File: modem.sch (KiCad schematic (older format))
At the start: 26 parts

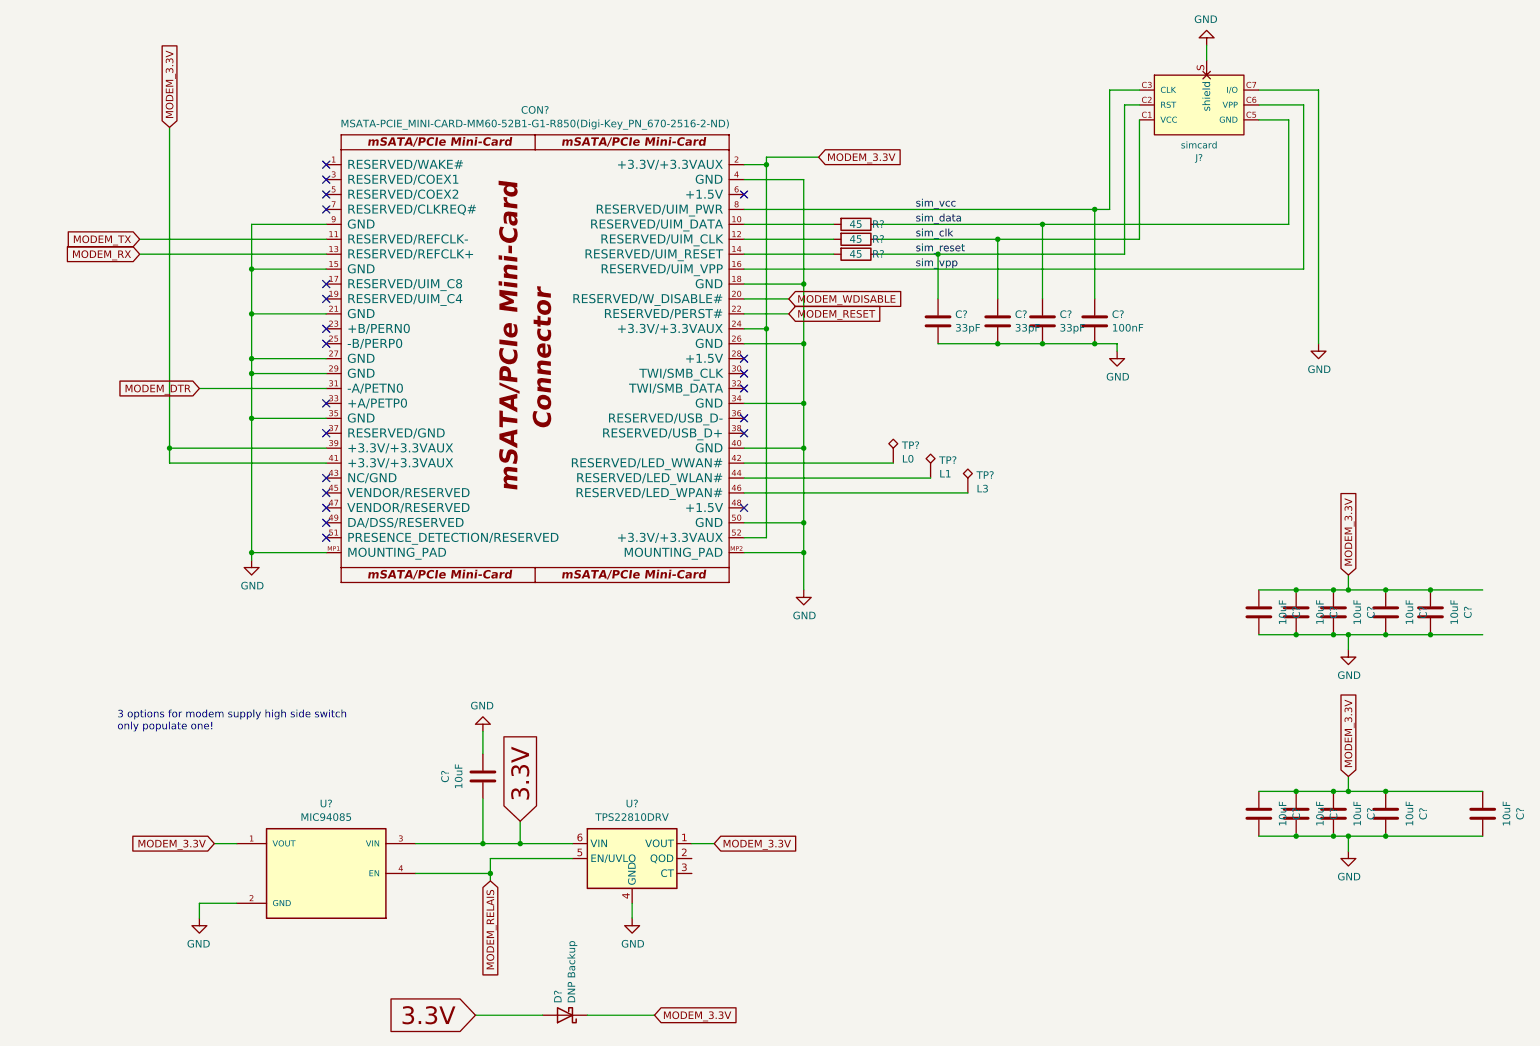
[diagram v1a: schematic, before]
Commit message: Esp32 & Canbus Sch. edited.
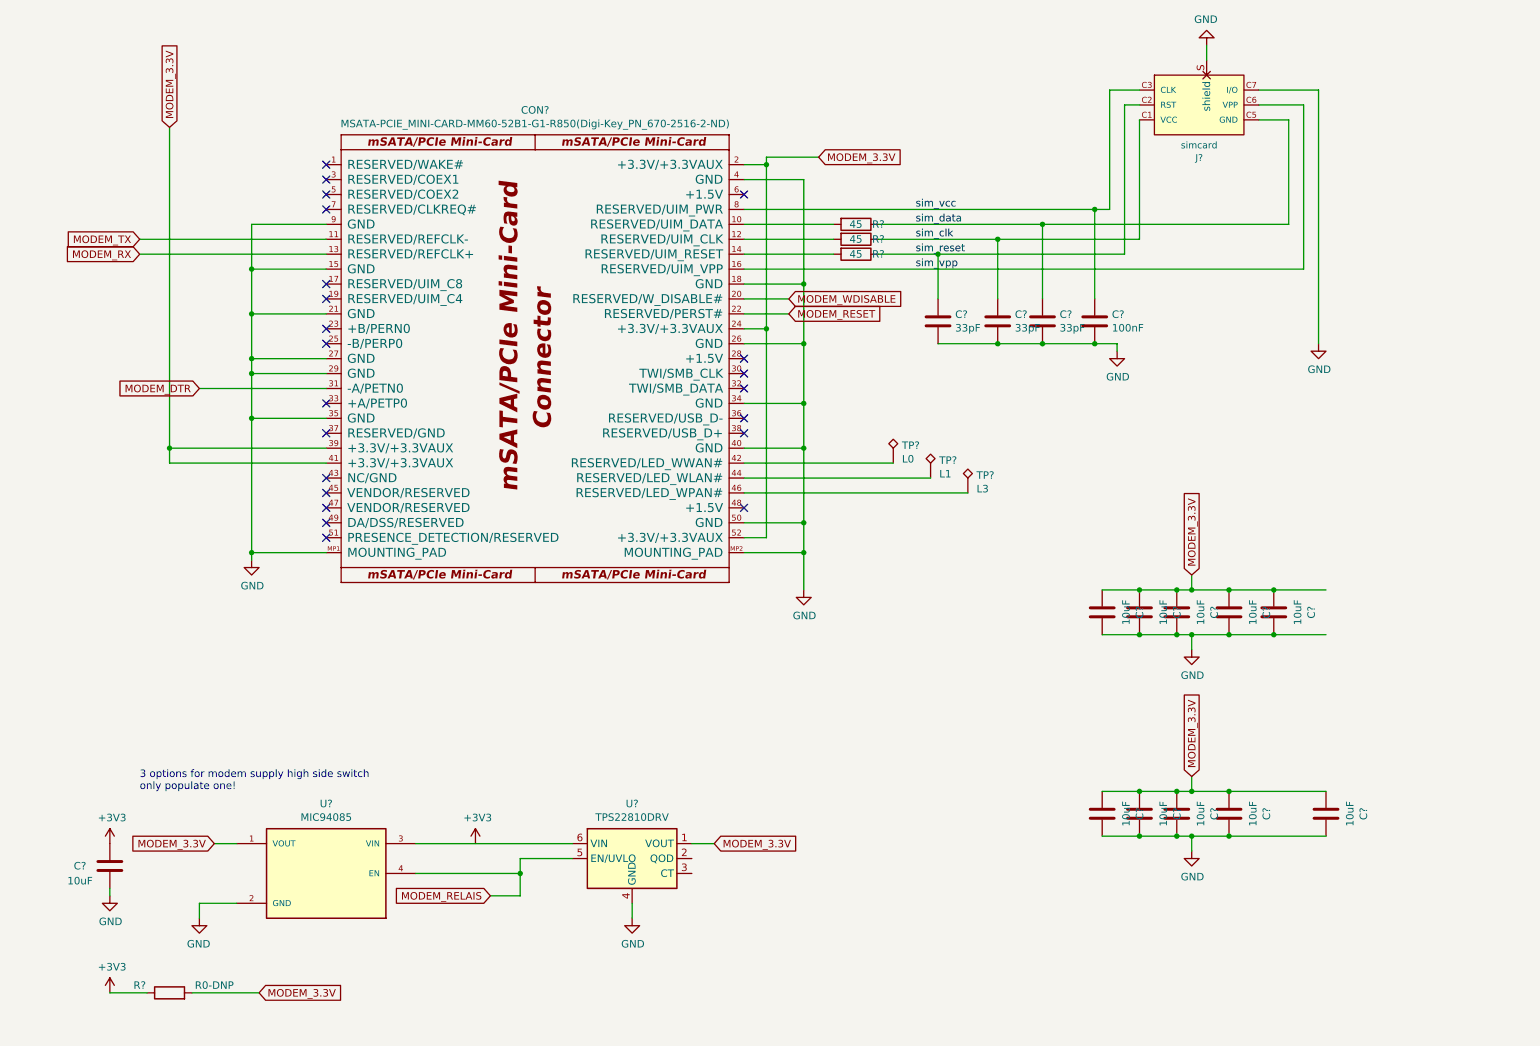
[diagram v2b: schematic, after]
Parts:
- removed C?: 10uF, Capacitor_SMD:C_1206_3216Metric, symbol Device:C
- removed D?: DNP Backup, Diode_SMD:D_SOD-123, symbol Device:D_Schottky
- added C?: 10uF, Capacitor_SMD:C_0603_1608Metric, symbol Device:C
- added R?: R0-DNP, Resistors:0603, symbol Device:R
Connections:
- net GND: now also C?.2
- net MODEM_3.3V: now also R?.2
- net 3.3V: no longer names the net of U?.3 (VIN), U?.6 (VIN)
- new net +3V3: C?.1, R?.1
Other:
- moved on the sheet: C?

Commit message: Modem schematic updated.
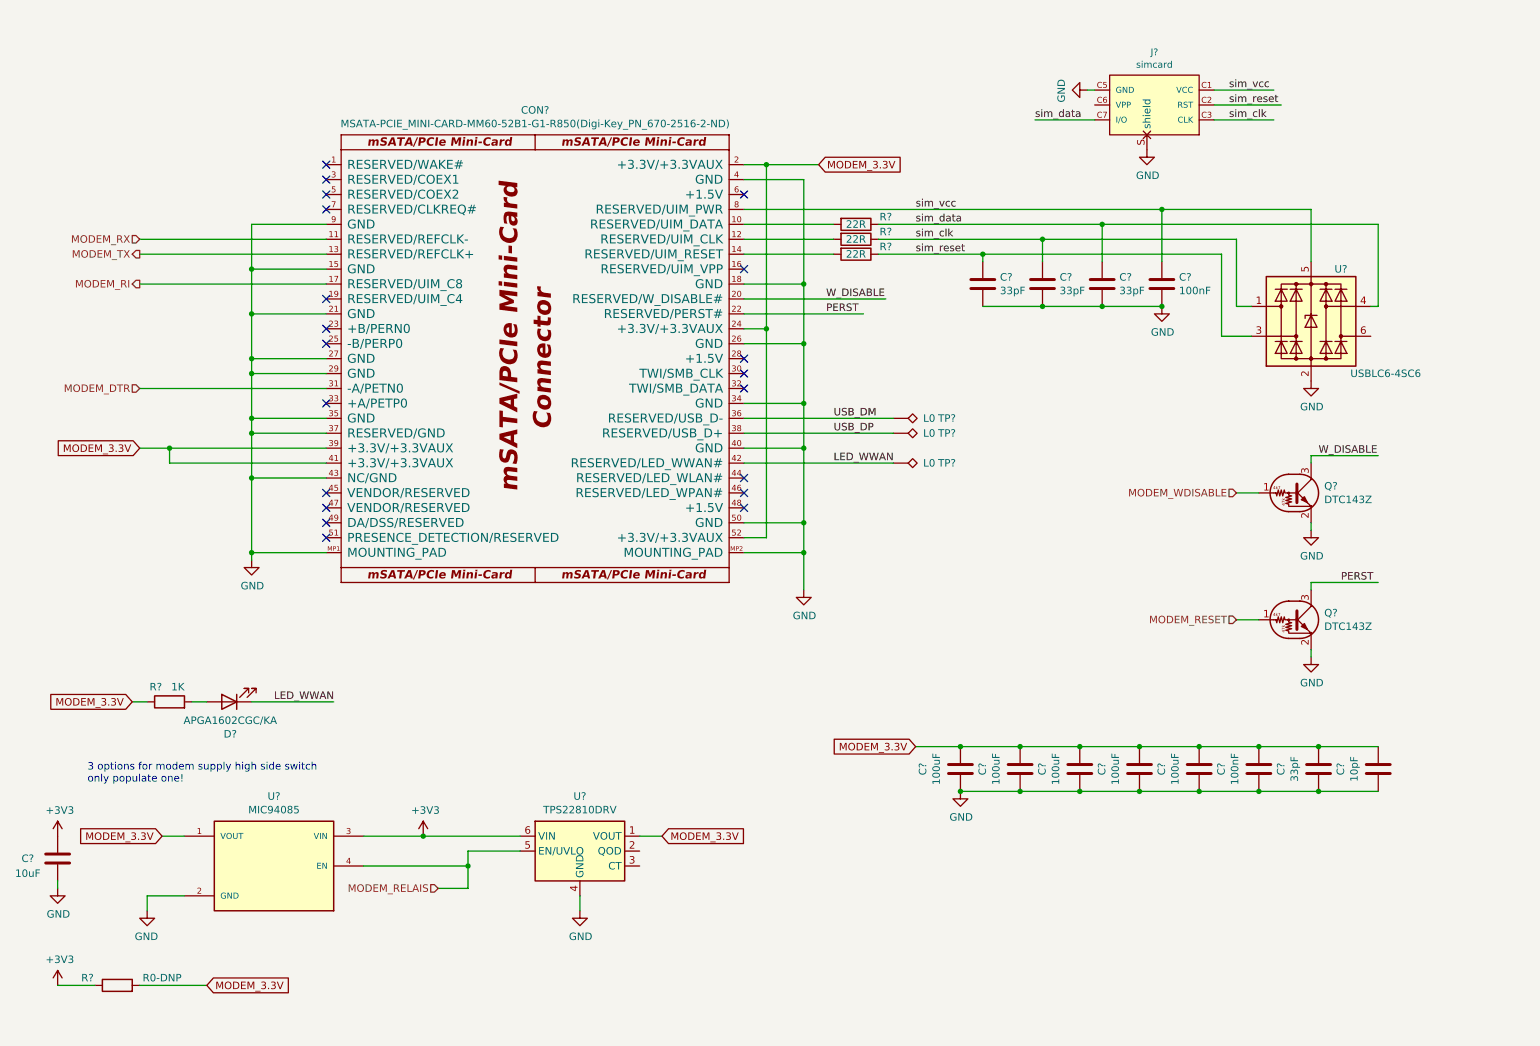
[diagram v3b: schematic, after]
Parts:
- removed C? (x10): 10uF, Capacitor_SMD:C_1206_3216Metric, symbol Device:C
- removed TP?: L0, OLIMEX_TestPoints-FP:TP_SMD, symbol Connector:TestPoint_Alt
- removed TP?: L1, OLIMEX_TestPoints-FP:TP_SMD, symbol Connector:TestPoint_Alt
- removed TP?: L3, OLIMEX_TestPoints-FP:TP_SMD, symbol Connector:TestPoint_Alt
- added C?: 10pF, Capacitor_SMD:C_0603_1608Metric, symbol Device:C
- added C?: 100nF, Capacitor_SMD:C_0603_1608Metric, symbol Device:C
- added C? (x5): 100uF, Capacitor_SMD:C_1206_3216Metric, symbol Device:C
- added C?: 33pF, Capacitor_SMD:C_0603_1608Metric, symbol Device:C
- added D?: APGA1602CGC/KA, LED_SMD:LED_0603_1608Metric, symbol Device:LED
- added Q? (x2): DTC143Z, symbol Transistor_BJT:DTC143Z
- added R?: 1K, Resistor_SMD:R_0603_1608Metric, symbol Device:R
- added TP? (x3): L0, OLIMEX_TestPoints-FP:TP_SMD, symbol Connector:TestPoint_Alt
- added U?: USBLC6-4SC6, Package_TO_SOT_SMD:SOT-23-6, symbol Power_Protection:USBLC6-4SC6
- R? (x3): value 45 -> 22R
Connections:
- net labels added: LED_WWAN, MODEM_RI, PERST, USB_DM, USB_DP, W_DISABLE
- net labels removed: sim_vpp
- wire segments 120 -> 122
- no-connect marks 22 -> 20
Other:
- moved on the sheet: C?, J?, R?, U?

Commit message: Power Sch. Updated.
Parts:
- gave numbers to parts that had none: 29

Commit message: Power section placement completed.
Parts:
- C51: renamed from C47; footprint Capacitors:0603 -> Capacitor_SMD:C_0603_1608Metric
- C53: renamed from C49; footprint Capacitors:0603 -> Capacitor_SMD:C_0603_1608Metric
- C55: renamed from C51; footprint Capacitors:0603 -> Capacitor_SMD:C_0603_1608Metric
- C57: renamed from C53; footprint Capacitors:0603 -> Capacitor_SMD:C_0603_1608Metric
- Q2, Q3: value DTC143Z -> MMUN2233LT1G; footprint (none) -> Package_TO_SOT_SMD:SOT-23
- R38: renamed from R34; footprint Resistors:0603 -> Resistor_SMD:R_0603_1608Metric
- R40: renamed from R36; footprint Resistors:0603 -> Resistor_SMD:R_0603_1608Metric
- R41: renamed from R37; footprint Resistors:0603 -> Resistor_SMD:R_0603_1608Metric
- R42: renamed from R38; footprint Resistors:0603 -> Resistor_SMD:R_0603_1608Metric
- TP10, TP8, TP9: footprint OLIMEX_TestPoints-FP:TP_SMD -> TestPoint:TestPoint_Pad_D1.0mm
- renumbered C45 to C49, C46 to C50, C48 to C52, C50 to C54, C52 to C56, C54 to C58, C55 to C59, C56 to C60, C57 to C61, R35 to R39

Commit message: Power section routing completed.
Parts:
- removed U11: MIC94085, aep:IC_MIC94080YFT-TR, symbol aep:MIC94080YFT-TR
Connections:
- wire segments 122 -> 116
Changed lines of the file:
@@
 Text GLabel 2450 7100 2    50   Input ~ 0
-MODEM_3.3V
-$Comp
-L aep:MIC94080YFT-TR U?
-U 1 1 6058AF0C
-P 2900 6300
-AR Path="/6058AF0C" Ref="U?"  Part="1"
-AR Path="/6055B0F2/6058AF0C" Ref="U11"  Part="1"
-F 0 "U11" H 2900 6767 50  0000 C CNN
-F 1 "MIC94085" H 2900 6676 50  0000 C CNN
-F 2 "aep:IC_MIC94080YFT-TR" H 2900 6300 50  0001 L BNN
-F 3 "" H 2900 6300 50  0001 L BNN
-F 4 "Manufacturer Recommendations" H 2900 6300 50  0001 L BNN "STANDARD"
-F 5 "A" H 2900 6300 50  0001 L BNN "PARTREV"
-F 6 "Microchip Technology" H 2900 6300 50  0001 L BNN "MANUFACTURER"
-F 7 "0.6 mm" H 2900 6300 50  0001 L BNN "MAXIMUM_PACKAGE_HEIGHT"
-	1    2900 6300
-	-1   0    0    -1
-$EndComp
-Wire Wire Line
-	2050 6500 2300 6500
-Wire Wire Line
-	2050 6600 2050 6500
-$Comp
-L power:GND #PWR?
-U 1 1 6058AF14
-P 2050 6600
-AR Path="/6058AF14" Ref="#PWR?"  Part="1"
-AR Path="/6055B0F2/6058AF14" Ref="#PWR088"  Part="1"
-F 0 "#PWR088" H 2050 6350 50  0001 C CNN
-F 1 "GND" H 2055 6427 50  0000 C CNN
-F 2 "" H 2050 6600 50  0001 C CNN
-F 3 "" H 2050 6600 50  0001 C CNN
-	1    2050 6600
-	-1   0    0    -1
-$EndComp
-Wire Wire Line
-	2150 6100 2300 6100
-Text GLabel 2150 6100 0    50   Input ~ 0
 MODEM_3.3V
 Text GLabel 5500 6100 2    50   Input ~ 0
@@
 $EndComp
 Wire Wire Line
-	3500 6300 4200 6300
-Wire Wire Line
-	4200 6300 4200 6200
-Wire Wire Line
 	4200 6200 4550 6200
 Wire Wire Line
-	4200 6300 4200 6450
-Wire Wire Line
 	4200 6450 4000 6450
-Connection ~ 4200 6300
 $Comp
 L Device:C C?
@@
 Wire Wire Line
 	1450 6400 1450 6450
-Wire Wire Line
-	3500 6100 3900 6100
 $Comp
 L power:+3V3 #PWR?
@@
 Wire Wire Line
 	1700 7100 1450 7100
-Connection ~ 3900 6100
 Wire Wire Line
 	3900 6100 4550 6100
@@
 Text HLabel 4000 6450 0    50   Input ~ 0
 MODEM_RELAIS
+Wire Wire Line
+	4200 6200 4200 6450
 $EndSCHEMATC

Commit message: PCB design updated.
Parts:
- removed TP10: L0, TestPoint:TestPoint_Pad_D1.0mm, symbol Connector:TestPoint_Alt
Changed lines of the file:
@@
 Wire Wire Line
 	6050 3600 7050 3600
-$Comp
-L Connector:TestPoint_Alt TP?
-U 1 1 6054A21C
-P 7050 3600
-AR Path="/6054A21C" Ref="TP?"  Part="1"
-AR Path="/6055B0F2/6054A21C" Ref="TP10"  Part="1"
-F 0 "TP10" V 7050 3900 50  0000 L CNN
-F 1 "L0" V 7050 3800 50  0000 L CNN
-F 2 "TestPoint:TestPoint_Pad_D1.0mm" H 7250 3600 50  0001 C CNN
-F 3 "~" H 7250 3600 50  0001 C CNN
-	1    7050 3600
-	0    1    1    0
-$EndComp
 Text Label 2900 5200 0    50   ~ 0
 LED_WWAN
